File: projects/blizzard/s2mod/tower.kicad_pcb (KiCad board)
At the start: 4 copper layers, 14 x 10 mm, 19 parts, among them U1 S2MOD_REV, U3 BALF-SPI2-01D3, Y1 24M

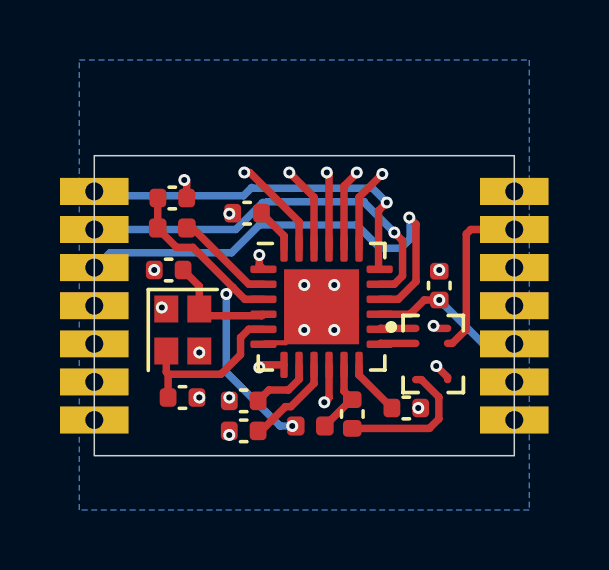
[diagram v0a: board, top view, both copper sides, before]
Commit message: Fix balun rotation in JLCPCB exports and change to LGA
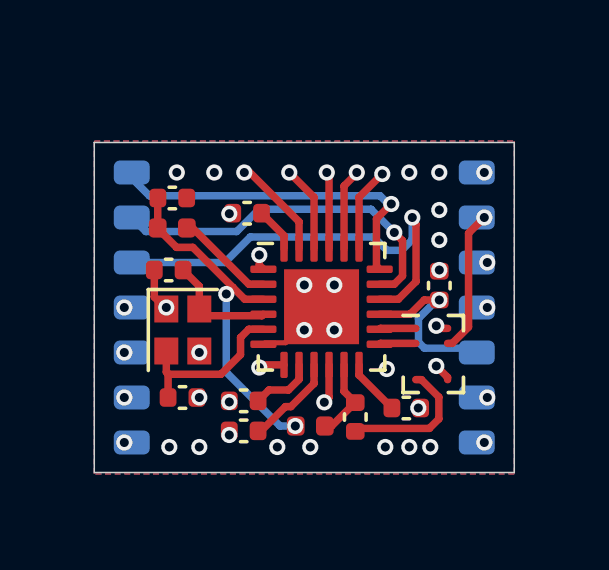
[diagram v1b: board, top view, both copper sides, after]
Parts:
- removed H1, H2, H3, H4: Tabs, kikit:Tab
- moved C1 0.14 mm to (81.7, 136.9)
- moved U1 0.06 mm to (80.0, 133.2)
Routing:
- net /RF_GPIO0: track 17.8 -> 15.2 mm, vias 1 -> 2
- net /RF_GPIO1: track 14.8 -> 13.1 mm, vias 1 -> 2
- net /RF_SDO: track 15.9 -> 14.5 mm
- net /RF_GPIO3: track 10.8 -> 9.56 mm, vias 1 -> 2
- net /RF_SDI: track 13.2 -> 12.0 mm
- net /RF_GPIO2: track 12.7 -> 11.5 mm, vias 1 -> 2
- net Net-(U1-ANT): track 5.66 -> 4.79 mm, vias 0 -> 1
- net /RF_SCL: track 12.5 -> 11.6 mm
- net +BATT: track 7.97 -> 8.72 mm
- net /RF_CSn: track 14.0 -> 13.4 mm, vias 1 -> 2
- net GND: track 4.37 -> 4.97 mm, vias 16 -> 32
- added copper zone on F.Cu, net GND
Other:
- board size 14 x 10 mm -> 14 x 11 mm
